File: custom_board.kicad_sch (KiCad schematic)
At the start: 1 part

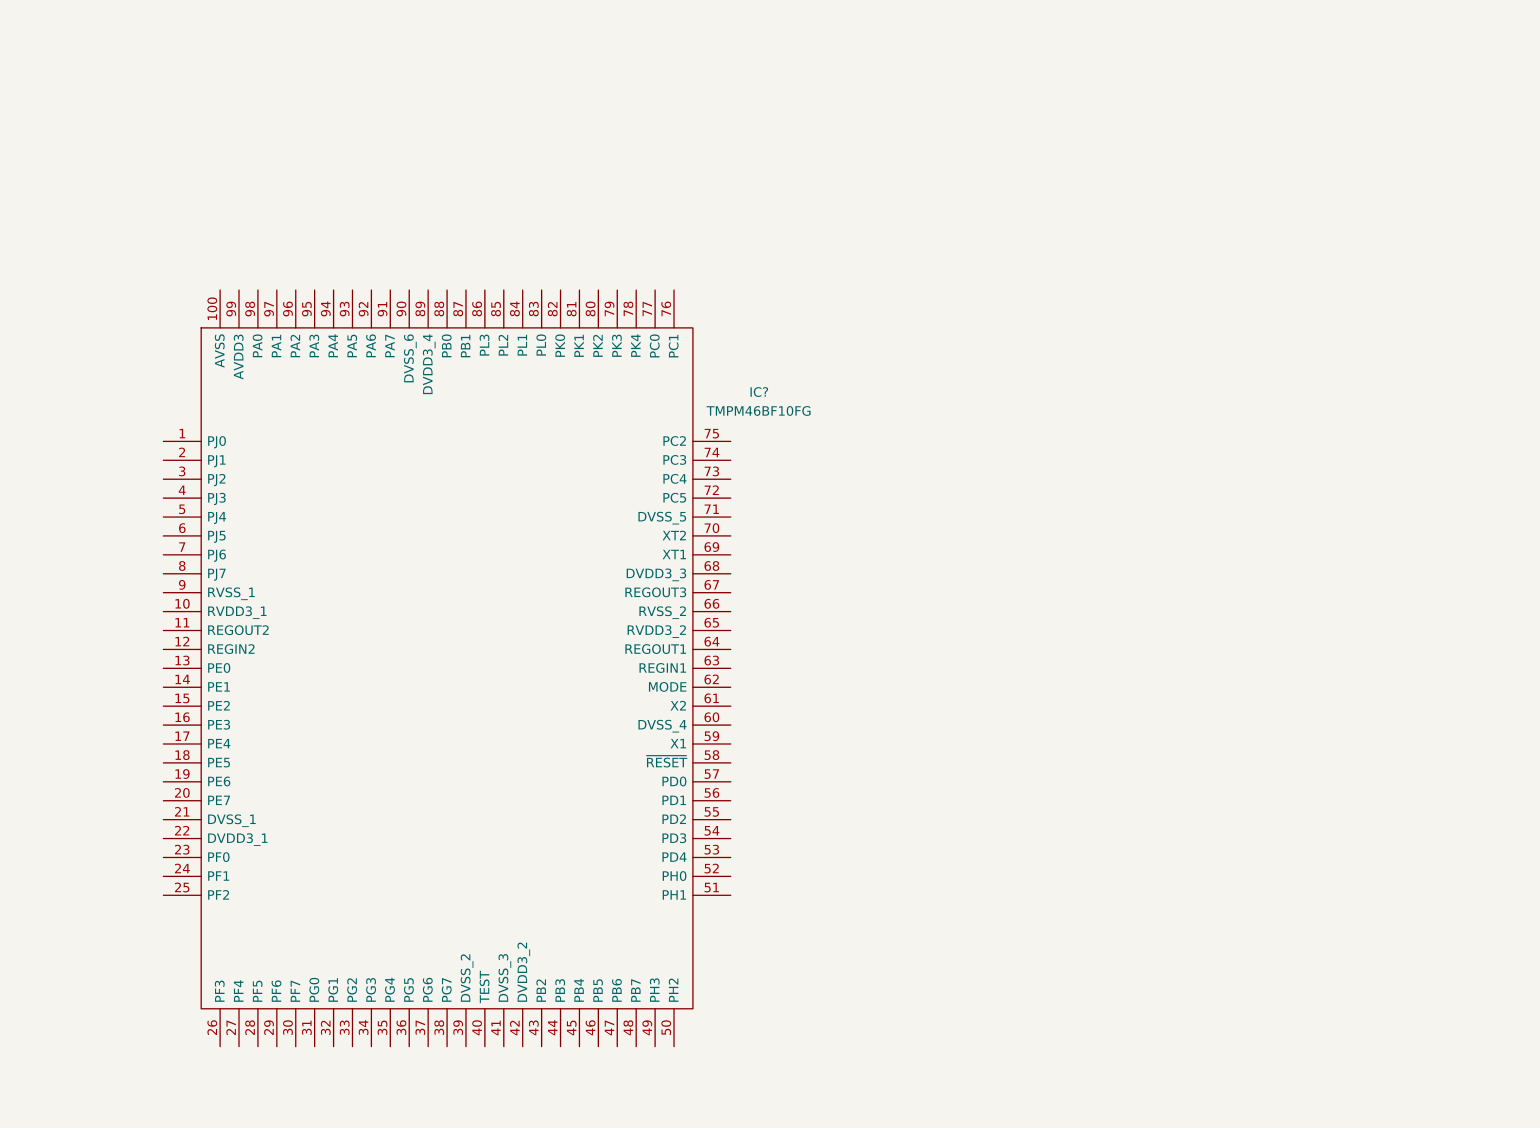
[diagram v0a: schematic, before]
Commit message: Updating footprint stuff
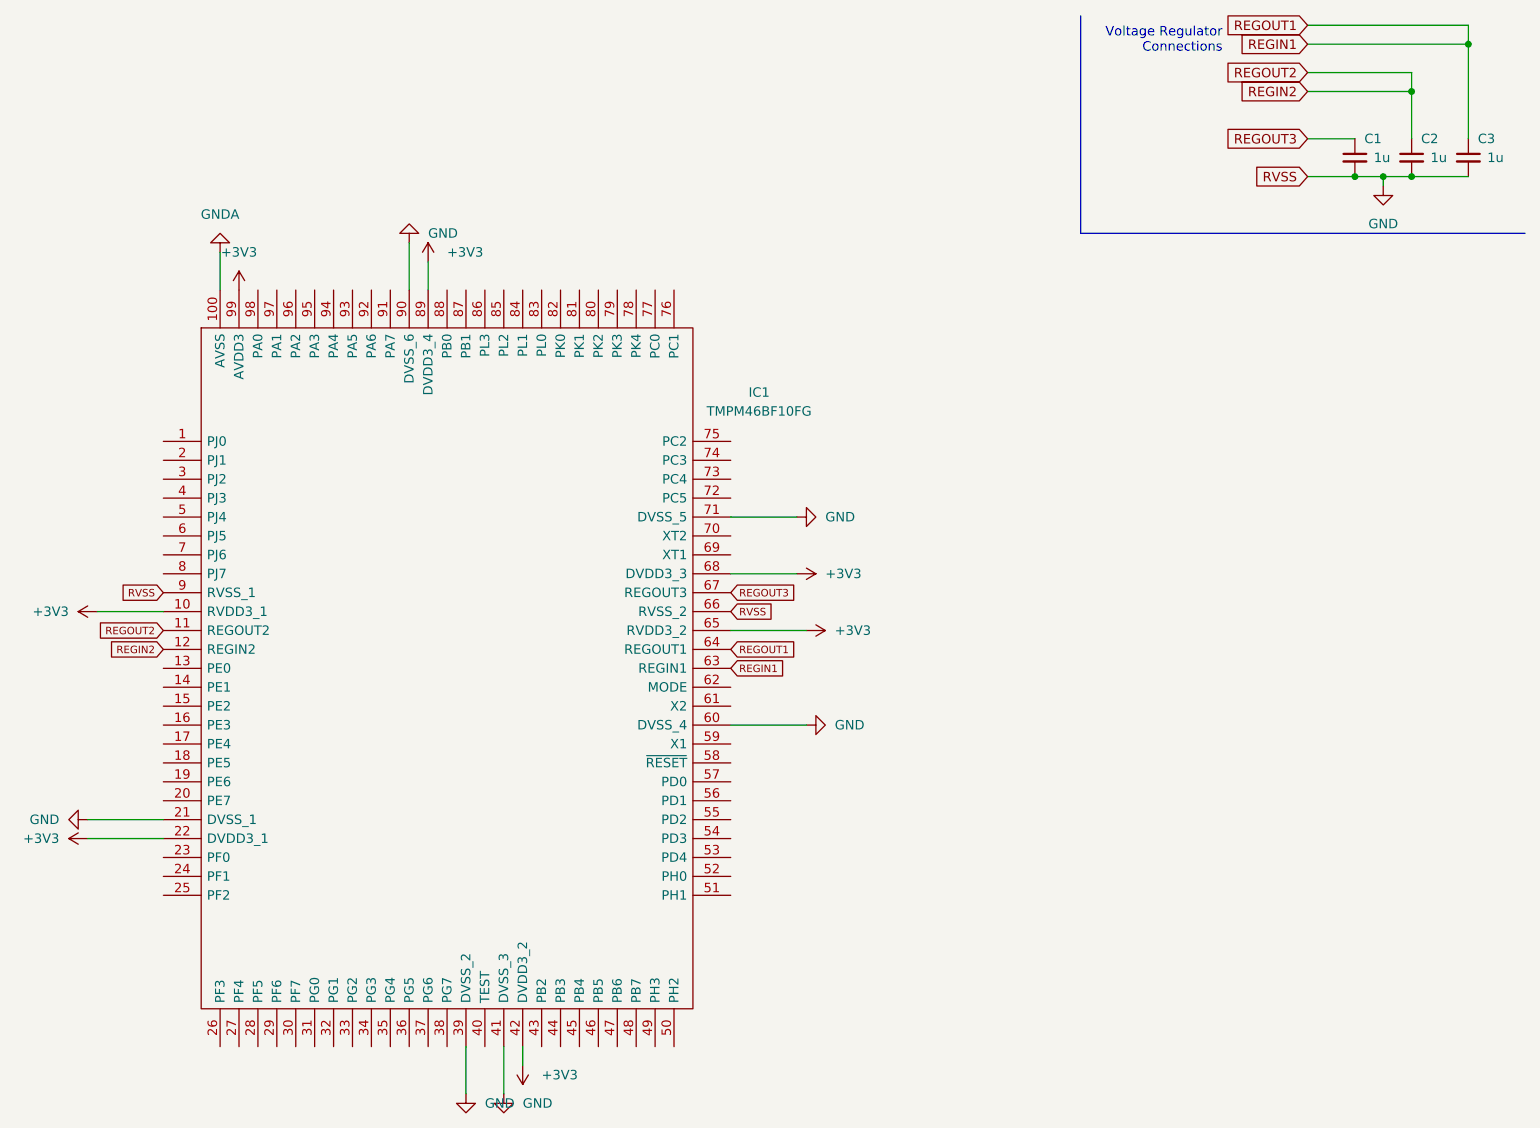
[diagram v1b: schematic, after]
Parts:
- added C1, C2, C3: 1u, Capacitor_SMD:C_0805_2012Metric, symbol Device:C_Small
- IC1: renamed from IC?; footprint QFP60P1600X1600X170-100N -> Package_DFN_QFN:TMPM_Custom_Footprint
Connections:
- net +3V3: now reaches IC1.10 (RVDD3_1)
- net +3V3: now also IC1.22 (DVDD3_1), IC1.42 (DVDD3_2), IC1.65 (RVDD3_2), IC1.68 (DVDD3_3), IC1.89 (DVDD3_4), IC1.99 (AVDD3)
- net GNDA: now reaches IC1.100 (AVSS)
- net REGIN2: now reaches IC1.11 (REGOUT2)
- net REGIN2: now also IC1.12 (REGIN2), C2.1
- net GND: now reaches IC1.21 (DVSS_1)
- net GND: now also IC1.39 (DVSS_2), IC1.41 (DVSS_3), IC1.60 (DVSS_4), IC1.66 (RVSS_2), IC1.71 (DVSS_5), IC1.9 (RVSS_1), IC1.90 (DVSS_6), C1.2, C2.2, C3.2
- net REGIN1: now reaches IC1.63 (REGIN1)
- net REGIN1: now also IC1.64 (REGOUT1), C3.1
- net REGOUT3: now reaches IC1.67 (REGOUT3)
- net REGOUT3: now also C1.1
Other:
- note added: "Voltage Regulator Connections"

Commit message: working on pin connections
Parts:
- added J?: Port A Conns, symbol Connector:Conn_01x08_Female
- added J?: Port C Conns, symbol Connector:Conn_01x06_Female
- added J?: Port F Conns, symbol Connector:Conn_01x08_Female
- added J?: Port G Conns, symbol Connector:Conn_01x08_Female
- added J?: Port B Conns, symbol Connector:Conn_01x08_Female
- added J?: Port D Conns, symbol Connector:Conn_01x05_Female
- added J?: Port E Conns, symbol Connector:Conn_01x08_Female
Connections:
- new net PA0: J?.1 (Pin_1)
- new net PA1: J?.2 (Pin_2)
- new net PA2: J?.3 (Pin_3)
- new net PA3: J?.4 (Pin_4)
- new net PA4: J?.5 (Pin_5)
- new net PA5: J?.6 (Pin_6)
- new net PA6: J?.7 (Pin_7)
- new net PA7: J?.8 (Pin_8)
- new net PB0: J?.1 (Pin_1)
- new net PB1: J?.2 (Pin_2)
- new net PB2: J?.3 (Pin_3)
- new net PB3: J?.4 (Pin_4)
- new net PB4: J?.5 (Pin_5)
- new net PB5: J?.6 (Pin_6)
- new net PB6: J?.7 (Pin_7)
- new net PB7: J?.8 (Pin_8)
- new net PC0: J?.1 (Pin_1)
- new net PC1: J?.2 (Pin_2)
- new net PC2: J?.3 (Pin_3)
- new net PC3: J?.4 (Pin_4)
- new net PC4: J?.5 (Pin_5)
- new net PC5: J?.6 (Pin_6)
- new net PD0: J?.1 (Pin_1)
- new net PD1: J?.2 (Pin_2)
- new net PD2: J?.3 (Pin_3)
- new net PD3: J?.4 (Pin_4)
- new net PD4: J?.5 (Pin_5)
- new net PE0: J?.1 (Pin_1)
- new net PE1: J?.2 (Pin_2)
- new net PE2: J?.3 (Pin_3)
- new net PE3: J?.4 (Pin_4)
- new net PE4: J?.5 (Pin_5)
- new net PE5: J?.6 (Pin_6)
- new net PE6: J?.7 (Pin_7)
- new net PE7: J?.8 (Pin_8)
- new net PF0: J?.1 (Pin_1)
- new net PF1: J?.2 (Pin_2)
- new net PF2: J?.3 (Pin_3)
- new net PF3: J?.4 (Pin_4)
- new net PF4: J?.5 (Pin_5)
- new net PF5: J?.6 (Pin_6)
- new net PF6: J?.7 (Pin_7)
- new net PF7: J?.8 (Pin_8)
- new net PG0: J?.1 (Pin_1)
- new net PG1: J?.2 (Pin_2)
- new net PG2: J?.3 (Pin_3)
- new net PG3: J?.4 (Pin_4)
- new net PG4: J?.5 (Pin_5)
- new net PG5: J?.6 (Pin_6)
- new net PG6: J?.7 (Pin_7)
- new net PG7: J?.8 (Pin_8)

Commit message: yup
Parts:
- added C? (x5): (no value), symbol Device:C_Small
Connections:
- net GNDA is gone; now on net GND: IC1.100 (AVSS)
- net GND: now also C?.2, C?.2, C?.2, C?.2, C?.2
- net +3V3 renamed 3v3Power
- net 3v3Power: now also C?.1, C?.1, C?.1, C?.1, C?.1; no longer IC1.99 (AVDD3)

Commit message: Update custom_board.kicad_sch
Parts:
- added C? (x2): 10p, symbol Device:C_Small
- added R?: 50, symbol Device:R
- added Y?: HighOscillator38.4M, symbol Device:Crystal
- C? (x4): value (none) -> 10u
- C?: value (none) -> 100n
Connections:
- net GND: now also IC1.65 (RVDD3_2)
- net at IC1.59 (X1): now also C?.1, Y?.1
- net at IC1.61 (X2): now also R?.1
- net 3v3Power renamed +3V3
- net +3V3: no longer IC1.65 (RVDD3_2)
- new net: C?.1, R?.2, Y?.2
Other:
- note added: "Crystal Caps = 2 * (CL - CStray)"
- note added: "Decoupling"
- moved on the sheet: C?

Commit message: Update custom_board.kicad_sch
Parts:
- removed C? (x2): 10p, symbol Device:C_Small
- removed C?: 100n, symbol Device:C_Small
- removed J?: Port A Conns, symbol Connector:Conn_01x08_Female
- removed J?: Port C Conns, symbol Connector:Conn_01x06_Female
- removed J?: Port F Conns, symbol Connector:Conn_01x08_Female
- removed J?: Port G Conns, symbol Connector:Conn_01x08_Female
- removed J?: Port B Conns, symbol Connector:Conn_01x08_Female
- removed J?: Port D Conns, symbol Connector:Conn_01x05_Female
- removed J?: Port E Conns, symbol Connector:Conn_01x08_Female
- removed R?: 50, symbol Device:R
- removed Y?: HighOscillator38.4M, symbol Device:Crystal
- added C10, C11, C12: .1u, symbol Device:C_Small
- added C4, C5: C_Small, symbol Device:C_Small
- added R1, R2: 47, symbol Device:R
- added Y1: 38Mhz, symbol Device:Crystal_GND24_Small
- added Y2: 32khz, symbol Device:Crystal_GND3_Small
- C6, C7, C8, C9: renamed from C?; value 10u -> .1u
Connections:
- net +3V3: now also IC1.99 (AVDD3), C10.1, C11.1, C12.1
- net GND: now also IC1.62 (MODE), C10.2, C11.2, C12.2, C4.2, C5.2, Y1.2, Y1.4, Y2.3
- net at IC1.59 (X1): now also Y2.1
- net at IC1.61 (X2): now also R2.1
- net at IC1.69 (XT1): now also C5.1, Y1.1
- net at IC1.70 (XT2): now also R1.1
- new net: R2.2, Y2.2
- new net: C4.1, R1.2, Y1.3
- no-connect marks 0 -> 1
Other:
- note added: "https://www.sensyst.co.jp/shop/user_data/TMPM46B/TMPM46BF10FG_cir_MP_2.pdf"
- note removed: "Crystal Caps = 2 * (CL - CStray)"
- moved on the sheet: C6, C7, C8, C9

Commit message: Update custom_board.kicad_sch
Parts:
- removed C4, C5: C_Small, symbol Device:C_Small
- removed R1, R2: 47, symbol Device:R
- removed Y1: 38Mhz, symbol Device:Crystal_GND24_Small
- removed Y2: 32khz, symbol Device:Crystal_GND3_Small
- added C? (x4): 10p, symbol Device:C_Small
- added R?: 47, symbol Device:R
- added Y?: LowOscillator, symbol Device:Crystal_Small
- added Y?: HighOscillator, symbol Device:Crystal_GND24_Small
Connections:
- net GND: now also C?.2, C?.2, C?.2, C?.2, Y?.2, Y?.4
- net at IC1.59 (X1): now also C?.1, Y?.1
- net at IC1.61 (X2): now also R?.1
- net at IC1.69 (XT1): now also C?.1, Y?.1
- net at IC1.70 (XT2): now also C?.1, Y?.2
- new net: C?.1, R?.2, Y?.3

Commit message: Working on hardware interfaces
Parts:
- added R2, R3: 10k, symbol Device:R
- added SW1: Boot Switch, symbol Switch:SW_SPST
- added SW2: Reset Button, symbol Switch:SW_Push
- gave numbers to parts that had none: 7
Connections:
- net +3V3: now also R2.2, R3.2
- net GND: now also SW1.2 (B), SW2.2
- net PJ0: now reaches IC1.1 (PJ0)
- net PE0: now reaches IC1.13 (PE0)
- net PE1: now reaches IC1.14 (PE1)
- net PE2: now reaches IC1.15 (PE2)
- net PE3: now reaches IC1.16 (PE3)
- net PE4: now reaches IC1.17 (PE4)
- net PE5: now reaches IC1.18 (PE5)
- net PE6: now reaches IC1.19 (PE6)
- net PJ1: now reaches IC1.2 (PJ1)
- net PE7: now reaches IC1.20 (PE7)
- net PF0: now reaches IC1.23 (PF0)
- net PF1: now reaches IC1.24 (PF1)
- net PF2: now reaches IC1.25 (PF2)
- net PF3: now reaches IC1.26 (PF3)
- net PF4: now reaches IC1.27 (PF4)
- net PF5: now reaches IC1.28 (PF5)
- net PF6: now reaches IC1.29 (PF6)
- net PJ2: now reaches IC1.3 (PJ2)
- net PF7: now reaches IC1.30 (PF7)
- net PG0: now reaches IC1.31 (PG0)
- net PG1: now reaches IC1.32 (PG1)
- net PG2: now reaches IC1.33 (PG2)
- net PG3: now reaches IC1.34 (PG3)
- net PG4: now reaches IC1.35 (PG4)
- net PG5: now reaches IC1.36 (PG5)
- net PG6: now reaches IC1.37 (PG6)
- net PG7: now reaches IC1.38 (PG7)
- net PJ3: now reaches IC1.4 (PJ3)
- net PB2: now reaches IC1.43 (PB2)
- net PB3: now reaches IC1.44 (PB3)
- net PB4: now reaches IC1.45 (PB4)
- net PB5: now reaches IC1.46 (PB5)
- net at IC1.47 (PB6): now also R2.1, SW1.1 (A)
- net PB7: now reaches IC1.48 (PB7)
- net PB8: now reaches IC1.49 (PH3)
- net PJ4: now reaches IC1.5 (PJ4)
- net PB9: now reaches IC1.50 (PH2)
- net PH1: now reaches IC1.51 (PH1)
- net PH0: now reaches IC1.52 (PH0)
- net PD4: now reaches IC1.53 (PD4)
- net PD3: now reaches IC1.54 (PD3)
- net PD2: now reaches IC1.55 (PD2)
- net PD1: now reaches IC1.56 (PD1)
- net PD0: now reaches IC1.57 (PD0)
- net at IC1.58 (~{RESET}): now also R3.1, SW2.1
- net PJ5: now reaches IC1.6 (PJ5)
- net PJ6: now reaches IC1.7 (PJ6)
- net PC5: now reaches IC1.72 (PC5)
- net PC4: now reaches IC1.73 (PC4)
- net PC3: now reaches IC1.74 (PC3)
- net PC2: now reaches IC1.75 (PC2)
- net PC1: now reaches IC1.76 (PC1)
- net PC0: now reaches IC1.77 (PC0)
- net PK4: now reaches IC1.78 (PK4)
- net PK3: now reaches IC1.79 (PK3)
- net PJ7: now reaches IC1.8 (PJ7)
- net PK2: now reaches IC1.80 (PK2)
- net PK1: now reaches IC1.81 (PK1)
- net PK0: now reaches IC1.82 (PK0)
- net PL0: now reaches IC1.83 (PL0)
- net PL1: now reaches IC1.84 (PL1)
- net PL2: now reaches IC1.85 (PL2)
- net PL3: now reaches IC1.86 (PL3)
- net PB1: now reaches IC1.87 (PB1)
- net PB0: now reaches IC1.88 (PB0)
- net PA7: now reaches IC1.91 (PA7)
- net PA6: now reaches IC1.92 (PA6)
- net PA5: now reaches IC1.93 (PA5)
- net PA4: now reaches IC1.94 (PA4)
- net PA4: now also IC1.95 (PA3)
- net PA2: now reaches IC1.96 (PA2)
- net PA1: now reaches IC1.97 (PA1)
- net PA0: now reaches IC1.98 (PA0)
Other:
- note added: "PB6 is BOOT! NEG LOGIC!"
- note added: "RESET IS NEG LOGIC!"
- title: (none) -> Toshiba UC Board Schematic
- moved on the sheet: C1, C10, C11, C12, C2, C3, C6, C7, C8, C9

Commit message: Update custom_board.kicad_sch
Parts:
- added J?: Port K, symbol Connector:Conn_01x05_Female
- added J?: Port E, symbol Connector:Conn_01x08_Female
- added J?: Port F, symbol Connector:Conn_01x08_Female
- added J?: Port L, symbol Connector:Conn_01x04_Female
- added J?: Port J, symbol Connector:Conn_01x08_Female
- added J?: Port H, symbol Connector:Conn_01x04_Female
- added J?: USB_UART Conn Pins, symbol Connector:Conn_01x05_Female
- added J?: Port A, symbol Connector:Conn_01x08_Female
- added J?: Port G, symbol Connector:Conn_01x08_Female
- added J?: Port B, symbol Connector:Conn_01x08_Female
- added J?: Port C, symbol Connector:Conn_01x06_Female
- added J?: Port D, symbol Connector:Conn_01x05_Female
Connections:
- net +3V3: now also J?.1 (Pin_1)
- net GND: now also J?.4 (Pin_4)
- net PA0: now also J?.1 (Pin_1)
- net PA1: now also J?.2 (Pin_2)
- net PA2: now also J?.3 (Pin_3)
- net PA4: now also J?.5 (Pin_5)
- net PA5: now also J?.6 (Pin_6)
- net PA6: now also J?.7 (Pin_7)
- net PA7: now also J?.8 (Pin_8)
- net PB0: now also J?.1 (Pin_1)
- net PB1: now also J?.2 (Pin_2)
- net PB2: now also J?.3 (Pin_3)
- net PB3: now also J?.4 (Pin_4)
- net PB4: now also J?.5 (Pin_5)
- net PB5: now also J?.6 (Pin_6)
- net PB7: now also J?.8 (Pin_8)
- net PC0: now also J?.1 (Pin_1)
- net PC1: now also J?.2 (Pin_2)
- net PC2: now also J?.3 (Pin_3)
- net PC3: now also J?.4 (Pin_4)
- net PC4: now also J?.5 (Pin_5)
- net PC5: now also J?.6 (Pin_6)
- net PE1 renamed RXD0
- net RXD0: now also J?.3 (Pin_3)
- net PE2 renamed TXD0
- net TXD0: now also J?.2 (Pin_2)
- new net PA3: J?.4 (Pin_4)
- no-connect marks 1 -> 3
